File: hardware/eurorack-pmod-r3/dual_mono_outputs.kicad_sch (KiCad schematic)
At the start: 12 parts, among them J7 PJ-302M0, J8 PJ-302M0, U4 TL074

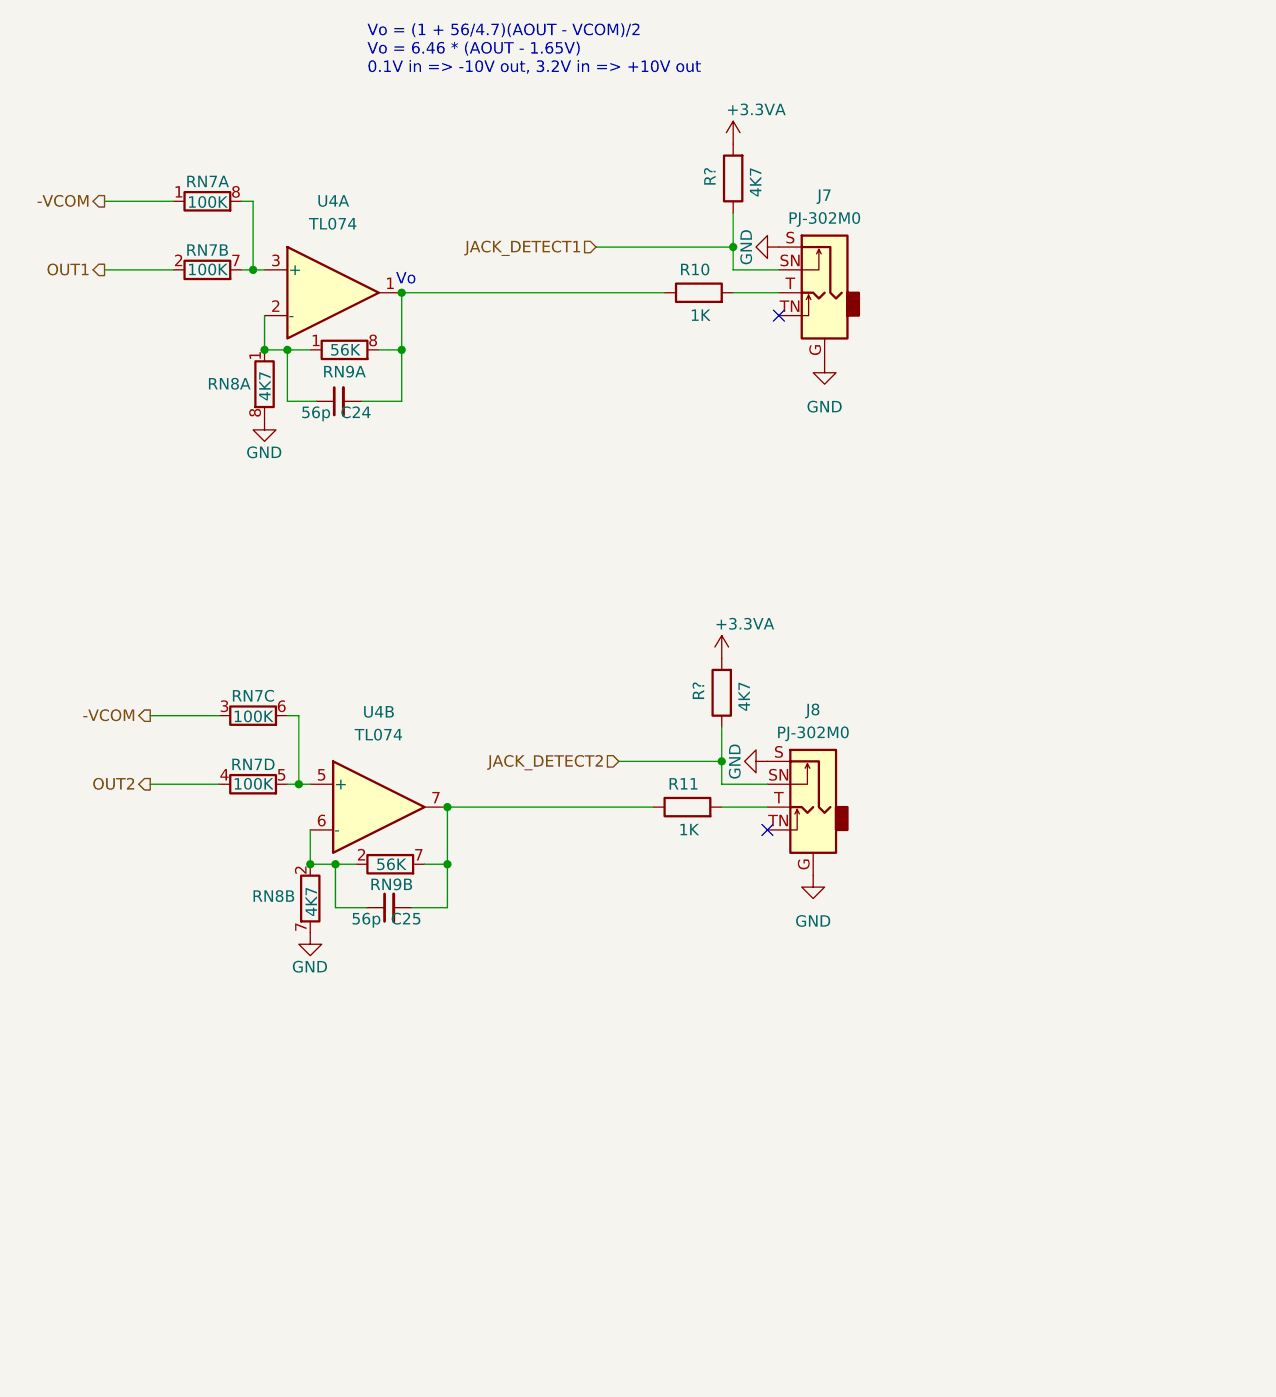
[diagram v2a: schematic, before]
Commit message: rev3/schematic: clean up with subsheets
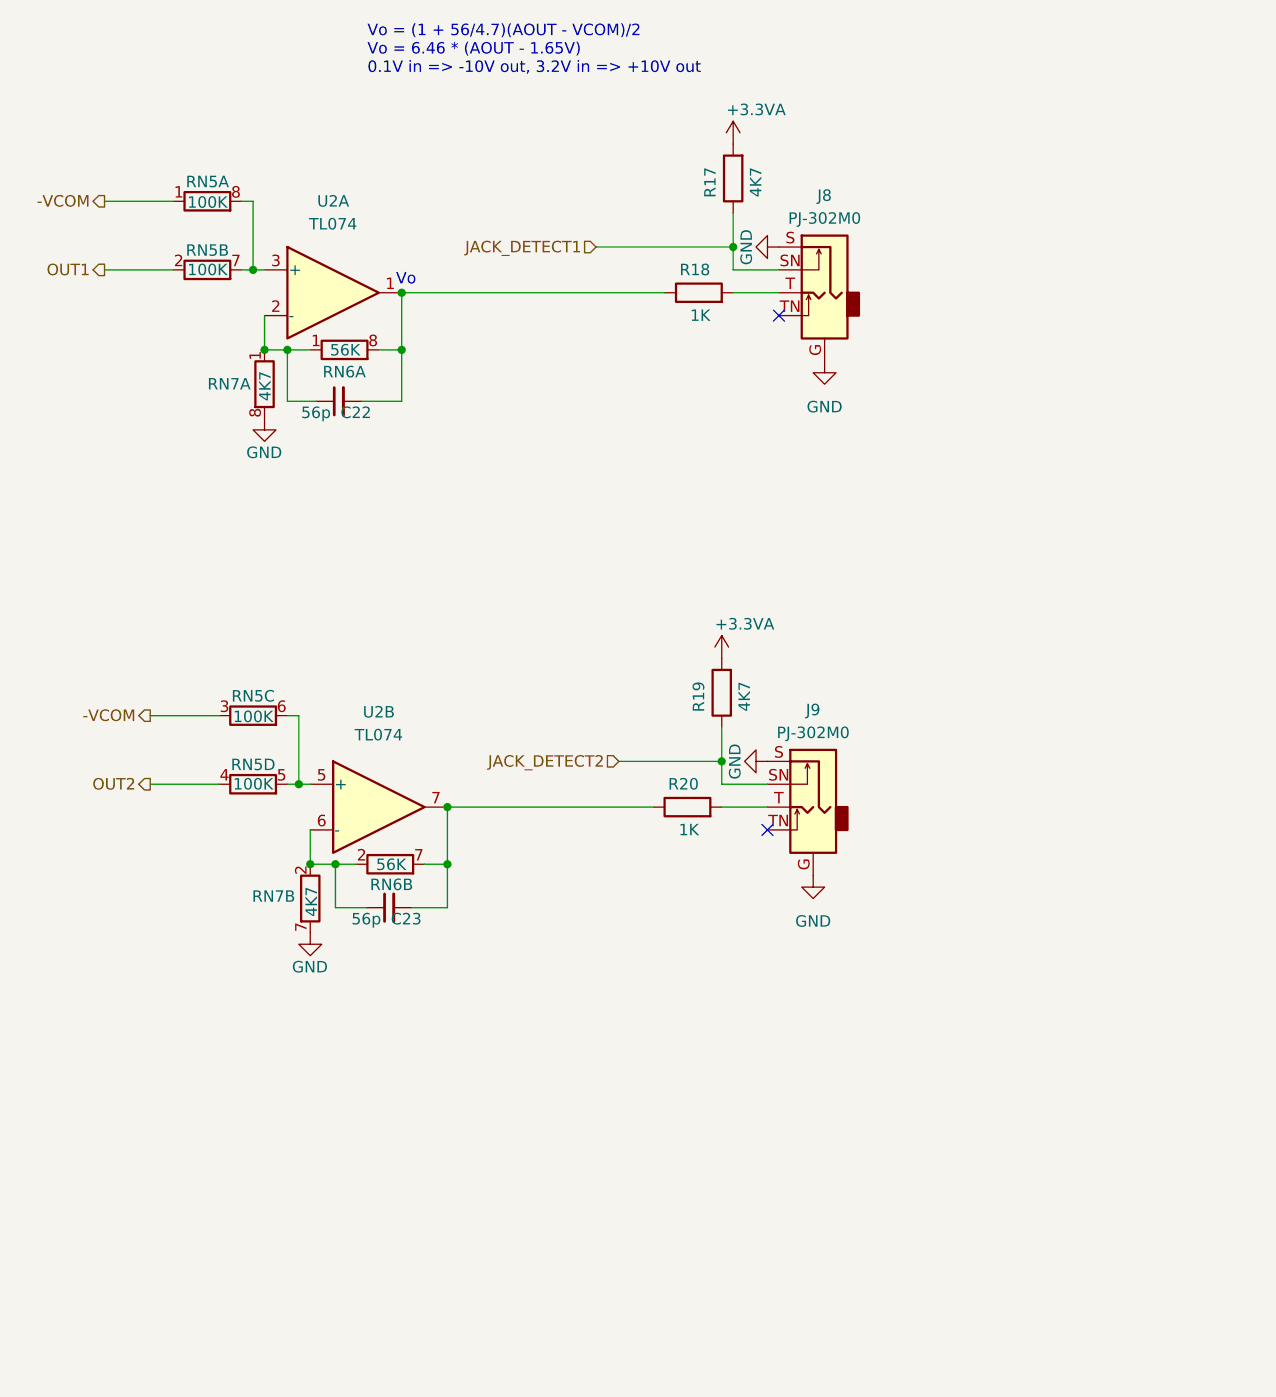
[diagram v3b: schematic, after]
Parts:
- gave numbers to parts that had none: 2
- renumbered C24 to C22, C25 to C23, J7 to J8, J8 to J9, R10 to R18, R11 to R20, RN7 to RN5, RN9 to RN6, RN8 to RN7, U4 to U2
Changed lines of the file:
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@@
   (symbol (lib_id "Device:R") (at 92.71 90.17 180) (unit 1)
     (in_bom yes) (on_board yes)
-    (property "Reference" "R?" (id 0) (at 90.17 88.9 90)
+    (property "Reference" "R19" (id 0) (at 90.17 88.9 90)
       (effects (font (size 1.27 1.27)) (justify left))
     )
@@
   (symbol (lib_id "Device:R_Pack04_Split") (at 40.64 92.71 270) (unit 3)
     (in_bom yes) (on_board yes)
-    (property "Reference" "RN7" (id 0) (at 40.64 90.551 90))
+    (property "Reference" "RN5" (id 0) (at 40.64 90.551 90))
     (property "Value" "100K" (id 1) (at 40.64 92.837 90))
     (property "Footprint" "Resistor_SMD:R_Cat16-4" (id 2) (at 40.64 90.678 90)
@@
   (symbol (lib_id "Device:R_Pack04_Split") (at 40.64 100.33 270) (unit 4)
     (in_bom yes) (on_board yes)
-    (property "Reference" "RN7" (id 0) (at 40.64 98.171 90))
+    (property "Reference" "RN5" (id 0) (at 40.64 98.171 90))
     (property "Value" "100K" (id 1) (at 40.64 100.33 90))
     (property "Footprint" "Resistor_SMD:R_Cat16-4" (id 2) (at 40.64 98.298 90)
@@
   (symbol (lib_id "power:GND") (at 97.79 97.79 270) (mirror x) (unit 1)
     (in_bom yes) (on_board yes)
-    (property "Reference" "#PWR?" (id 0) (at 91.44 97.79 0)
+    (property "Reference" "#PWR082" (id 0) (at 91.44 97.79 0)
       (effects (font (size 1.27 1.27)) hide)
     )
@@
   (symbol (lib_id "power:GND") (at 102.87 110.49 0) (mirror y) (unit 1)
     (in_bom yes) (on_board yes) (fields_autoplaced)
-    (property "Reference" "#PWR059" (id 0) (at 102.87 116.84 0)
+    (property "Reference" "#PWR083" (id 0) (at 102.87 116.84 0)
       (effects (font (size 1.27 1.27)) hide)
     )
@@
   (symbol (lib_id "Device:R_Pack04_Split") (at 35.56 43.18 270) (unit 2)
     (in_bom yes) (on_board yes)
-    (property "Reference" "RN7" (id 0) (at 35.56 41.021 90))
+    (property "Reference" "RN5" (id 0) (at 35.56 41.021 90))
     (property "Value" "100K" (id 1) (at 35.56 43.18 90))
     (property "Footprint" "Resistor_SMD:R_Cat16-4" (id 2) (at 35.56 41.148 90)
@@
   (symbol (lib_id "Device:R_Pack04_Split") (at 41.91 55.88 180) (unit 1)
     (in_bom yes) (on_board yes)
-    (property "Reference" "RN8" (id 0) (at 35.56 55.88 0)
+    (property "Reference" "RN7" (id 0) (at 35.56 55.88 0)
       (effects (font (size 1.27 1.27)) (justify right))
     )
@@
   (symbol (lib_id "Device:R") (at 90.17 45.72 90) (unit 1)
     (in_bom yes) (on_board yes)
-    (property "Reference" "R10" (id 0) (at 91.44 43.18 90)
+    (property "Reference" "R18" (id 0) (at 91.44 43.18 90)
       (effects (font (size 1.27 1.27)) (justify left))
     )
@@
   (symbol (lib_id "power:GND") (at 41.91 59.69 0) (unit 1)
     (in_bom yes) (on_board yes)
-    (property "Reference" "#PWR070" (id 0) (at 41.91 66.04 0)
+    (property "Reference" "#PWR080" (id 0) (at 41.91 66.04 0)
       (effects (font (size 1.27 1.27)) hide)
     )
@@
   (symbol (lib_id "Connector:AudioJack2_Ground_Switch") (at 104.14 45.72 0) (mirror y) (unit 1)
     (in_bom yes) (on_board yes)
-    (property "Reference" "J7" (id 0) (at 104.14 34.925 0))
+    (property "Reference" "J8" (id 0) (at 104.14 34.925 0))
     (property "Value" "PJ-302M0" (id 1) (at 104.14 37.465 0))
     (property "Footprint" "AudioJacksFixed:pj324m" (id 2) (at 104.14 40.64 0)
@@
   (symbol (lib_id "Connector:AudioJack2_Ground_Switch") (at 102.87 102.87 0) (mirror y) (unit 1)
     (in_bom yes) (on_board yes)
-    (property "Reference" "J8" (id 0) (at 102.87 92.075 0))
+    (property "Reference" "J9" (id 0) (at 102.87 92.075 0))
     (property "Value" "PJ-302M0" (id 1) (at 102.87 94.615 0))
     (property "Footprint" "AudioJacksFixed:pj324m" (id 2) (at 102.87 97.79 0)
@@
   (symbol (lib_id "Device:R_Pack04_Split") (at 46.99 113.03 180) (unit 2)
     (in_bom yes) (on_board yes)
-    (property "Reference" "RN8" (id 0) (at 40.5126 112.803 0)
+    (property "Reference" "RN7" (id 0) (at 40.5126 112.803 0)
       (effects (font (size 1.27 1.27)) (justify right))
     )
@@
   (symbol (lib_id "Device:R_Pack04_Split") (at 50.8 52.07 270) (unit 1)
     (in_bom yes) (on_board yes)
-    (property "Reference" "RN9" (id 0) (at 50.7619 54.5301 90))
+    (property "Reference" "RN6" (id 0) (at 50.7619 54.5301 90))
     (property "Value" "56K" (id 1) (at 50.8525 52.1025 90))
     (property "Footprint" "Resistor_SMD:R_Cat16-4" (id 2) (at 50.8 50.038 90)
@@
   (symbol (lib_id "power:GND") (at 104.14 53.34 0) (mirror y) (unit 1)
     (in_bom yes) (on_board yes) (fields_autoplaced)
-    (property "Reference" "#PWR056" (id 0) (at 104.14 59.69 0)
+    (property "Reference" "#PWR079" (id 0) (at 104.14 59.69 0)
       (effects (font (size 1.27 1.27)) hide)
     )
@@
   (symbol (lib_id "Device:R") (at 93.98 33.02 180) (unit 1)
     (in_bom yes) (on_board yes)
-    (property "Reference" "R?" (id 0) (at 91.44 31.75 90)
+    (property "Reference" "R17" (id 0) (at 91.44 31.75 90)
       (effects (font (size 1.27 1.27)) (justify left))
     )
@@
   (symbol (lib_id "Device:R_Pack04_Split") (at 55.88 109.22 270) (unit 2)
     (in_bom yes) (on_board yes)
-    (property "Reference" "RN9" (id 0) (at 56.0238 111.5023 90))
+    (property "Reference" "RN6" (id 0) (at 56.0238 111.5023 90))
     (property "Value" "56K" (id 1) (at 55.9694 109.2739 90))
     (property "Footprint" "Resistor_SMD:R_Cat16-4" (id 2) (at 55.88 107.188 90)
@@
   (symbol (lib_id "power:GND") (at 99.06 40.64 270) (mirror x) (unit 1)
     (in_bom yes) (on_board yes)
-    (property "Reference" "#PWR?" (id 0) (at 92.71 40.64 0)
+    (property "Reference" "#PWR078" (id 0) (at 92.71 40.64 0)
       (effects (font (size 1.27 1.27)) hide)
     )
@@
   (symbol (lib_id "Amplifier_Operational:TL074") (at 54.61 102.87 0) (unit 2)
     (in_bom yes) (on_board yes) (fields_autoplaced)
-    (property "Reference" "U4" (id 0) (at 54.61 92.329 0))
+    (property "Reference" "U2" (id 0) (at 54.61 92.329 0))
     (property "Value" "TL074" (id 1) (at 54.61 94.869 0))
     (property "Footprint" "Package_SO:TSSOP-14_4.4x5mm_P0.65mm" (id 2) (at 53.34 100.33 0)
@@
   (symbol (lib_id "Device:R_Pack04_Split") (at 35.56 35.56 270) (unit 1)
     (in_bom yes) (on_board yes)
-    (property "Reference" "RN7" (id 0) (at 35.56 33.401 90))
+    (property "Reference" "RN5" (id 0) (at 35.56 33.401 90))
     (property "Value" "100K" (id 1) (at 35.56 35.687 90))
     (property "Footprint" "Resistor_SMD:R_Cat16-4" (id 2) (at 35.56 33.528 90)
@@
   (symbol (lib_id "power:+3.3VA") (at 92.71 86.36 0) (unit 1)
     (in_bom yes) (on_board yes)
-    (property "Reference" "#PWR?" (id 0) (at 92.71 90.17 0)
+    (property "Reference" "#PWR081" (id 0) (at 92.71 90.17 0)
       (effects (font (size 1.27 1.27)) hide)
     )
@@
   (symbol (lib_id "power:GND") (at 46.99 116.84 0) (unit 1)
     (in_bom yes) (on_board yes)
-    (property "Reference" "#PWR075" (id 0) (at 46.99 123.19 0)
+    (property "Reference" "#PWR084" (id 0) (at 46.99 123.19 0)
       (effects (font (size 1.27 1.27)) hide)
     )
@@
   (symbol (lib_id "Device:R") (at 88.9 102.87 90) (unit 1)
     (in_bom yes) (on_board yes)
-    (property "Reference" "R11" (id 0) (at 90.17 100.33 90)
+    (property "Reference" "R20" (id 0) (at 90.17 100.33 90)
       (effects (font (size 1.27 1.27)) (justify left))
     )
@@
   (symbol (lib_id "Amplifier_Operational:TL074") (at 49.53 45.72 0) (unit 1)
     (in_bom yes) (on_board yes) (fields_autoplaced)
-    (property "Reference" "U4" (id 0) (at 49.53 35.56 0))
+    (property "Reference" "U2" (id 0) (at 49.53 35.56 0))
     (property "Value" "TL074" (id 1) (at 49.53 38.1 0))
     (property "Footprint" "Package_SO:TSSOP-14_4.4x5mm_P0.65mm" (id 2) (at 48.26 43.18 0)
@@
   (symbol (lib_id "Device:C_Small") (at 50.165 57.785 90) (unit 1)
     (in_bom yes) (on_board yes)
-    (property "Reference" "C24" (id 0) (at 52.07 59.055 90))
+    (property "Reference" "C22" (id 0) (at 52.07 59.055 90))
     (property "Value" "56p" (id 1) (at 47.625 59.055 90))
     (property "Footprint" "Capacitor_SMD:C_0603_1608Metric" (id 2) (at 50.165 57.785 0)
@@
   (symbol (lib_id "Device:C_Small") (at 55.753 114.046 90) (unit 1)
     (in_bom yes) (on_board yes)
-    (property "Reference" "C25" (id 0) (at 57.658 115.316 90))
+    (property "Reference" "C23" (id 0) (at 57.658 115.316 90))
     (property "Value" "56p" (id 1) (at 53.213 115.316 90))
     (property "Footprint" "Capacitor_SMD:C_0603_1608Metric" (id 2) (at 55.753 114.046 0)
@@
   (symbol (lib_id "power:+3.3VA") (at 93.98 29.21 0) (unit 1)
     (in_bom yes) (on_board yes)
-    (property "Reference" "#PWR?" (id 0) (at 93.98 33.02 0)
-      (effects (font (size 1.27 1.27)) hide)
-    )
+    (property "Reference" "#PWR077" (id 0) (at 93.98 33.02 0)
+      (effects (font (size 1.27 1.27)) hide)
+    )

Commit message: rev3/schematic: add PN and footprint for most components
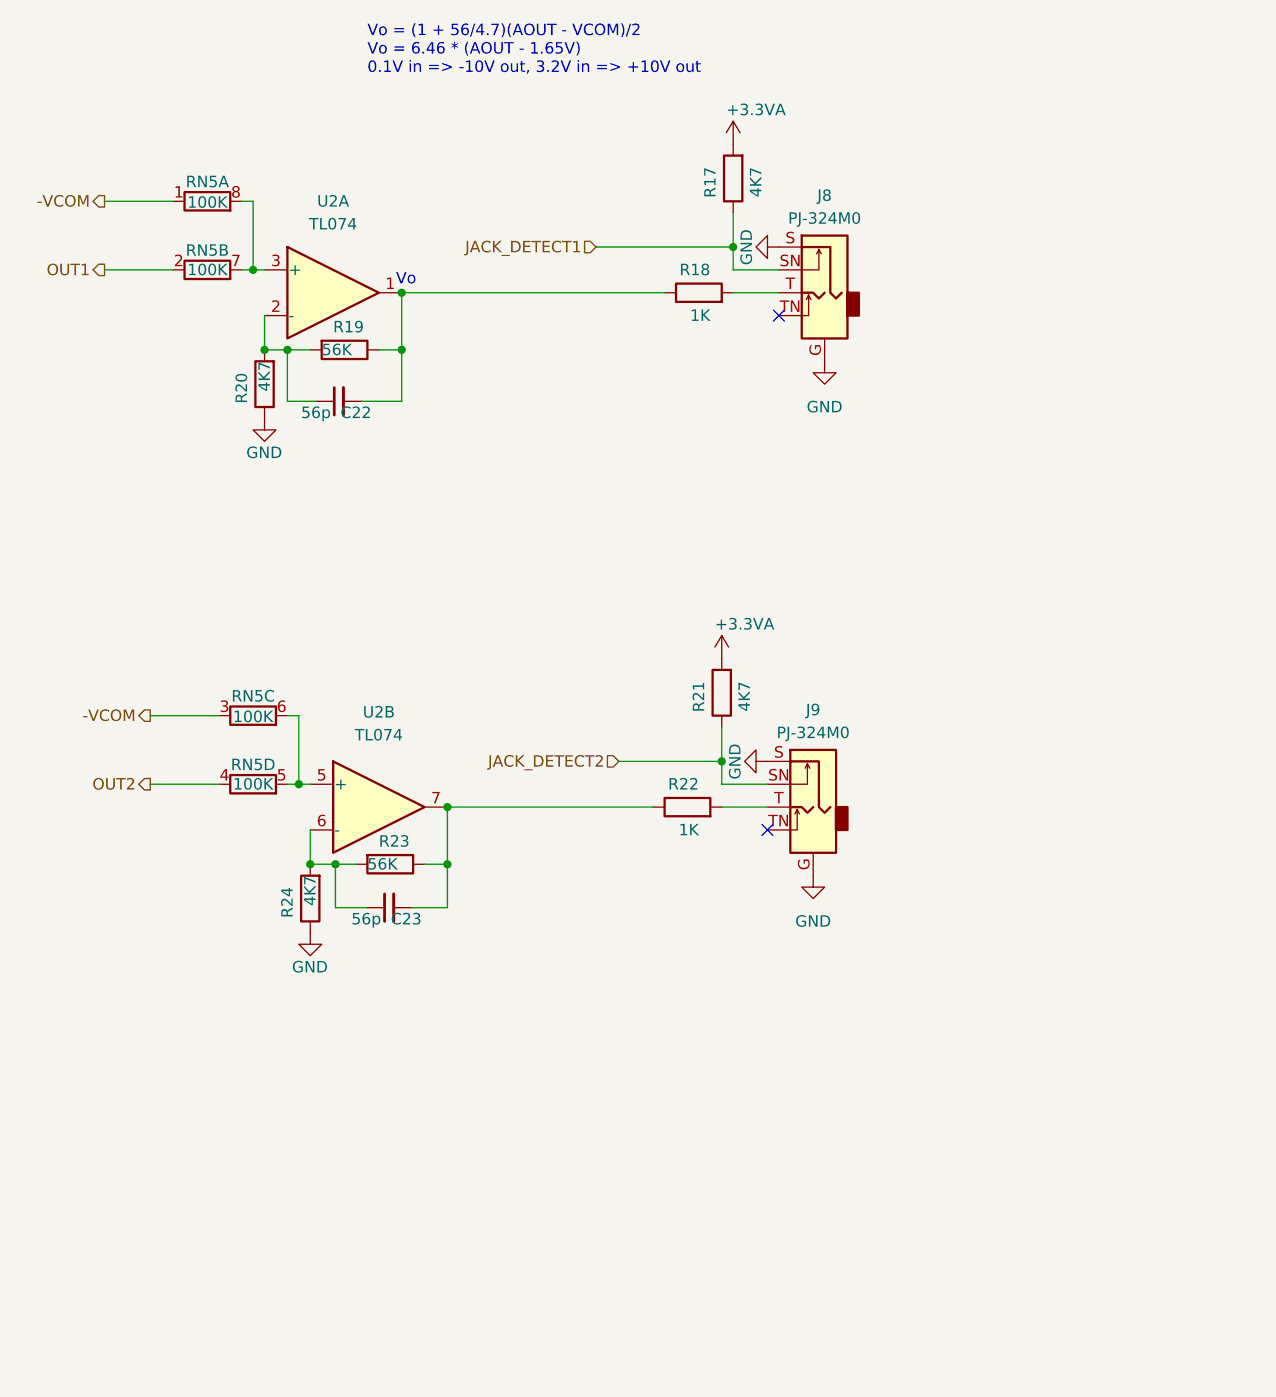
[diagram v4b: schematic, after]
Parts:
- removed RN6: 56K, Resistor_SMD:R_Cat16-4, symbol Device:R_Pack04_Split
- removed RN7: 4K7, Resistor_SMD:R_Cat16-4, symbol Device:R_Pack04_Split
- added R19, R23: 56K, Resistor_SMD:R_0402_1005Metric, symbol Device:R
- added R20, R24: 4K7, Resistor_SMD:R_0402_1005Metric, symbol Device:R
- C22, C23: footprint Capacitor_SMD:C_0603_1608Metric -> Capacitor_SMD:C_0402_1005Metric; lcsc# (none) -> C526981; mfg# (none) -> CC0402FRNPO9BN560
- J8, J9: value PJ-302M0 -> PJ-324M0; lcsc# (none) -> C2884986; mfg# (none) -> PJ-324M0
- R17: footprint Resistor_SMD:R_0603_1608Metric -> Resistor_SMD:R_0402_1005Metric; lcsc# (none) -> C105871; mfg# (none) -> RC0402FR-074K7L
- R18: lcsc# (none) -> C22548; mfg# (none) -> RC0603FR-071KL
- R21: renamed from R19; footprint Resistor_SMD:R_0603_1608Metric -> Resistor_SMD:R_0402_1005Metric; lcsc# (none) -> C105871; mfg# (none) -> RC0402FR-074K7L
- R22: renamed from R20; lcsc# (none) -> C22548; mfg# (none) -> RC0603FR-071KL
- RN5: footprint Resistor_SMD:R_Cat16-4 -> Resistor_SMD:R_Array_Convex_4x0402; dig# CAT16-1003F4LFCT-ND -> (none); lcsc# (none) -> C326786; mfg# CAT16-1003F4LF -> YC124-FR-07100KL
- U2: footprint Package_SO:TSSOP-14_4.4x5mm_P0.65mm -> Package_SO:SOIC-14_3.9x8.7mm_P1.27mm; dig# 296-26697-5-ND -> 497-2204-1-ND; lcsc# (none) -> C6963; mfg# TL074CPW -> TL074CDT
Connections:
- net GND: now also R20.1, R24.1
- net at C22.1, U2.2 (-): now also R19.2, R20.2
- net at C22.2, R18.1, U2.1: now also R19.1
- net at C23.1, U2.6 (-): now also R23.2, R24.2
- net at C23.2, R22.1, U2.7: now also R23.1
